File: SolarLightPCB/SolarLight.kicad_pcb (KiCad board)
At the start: 2 copper layers, 100 x 45 mm, 17 parts, among them J1 I2C, J2 SPI, U1 TP4056, U2 WeMos_D1_mini, U3 MCP1700-3302E

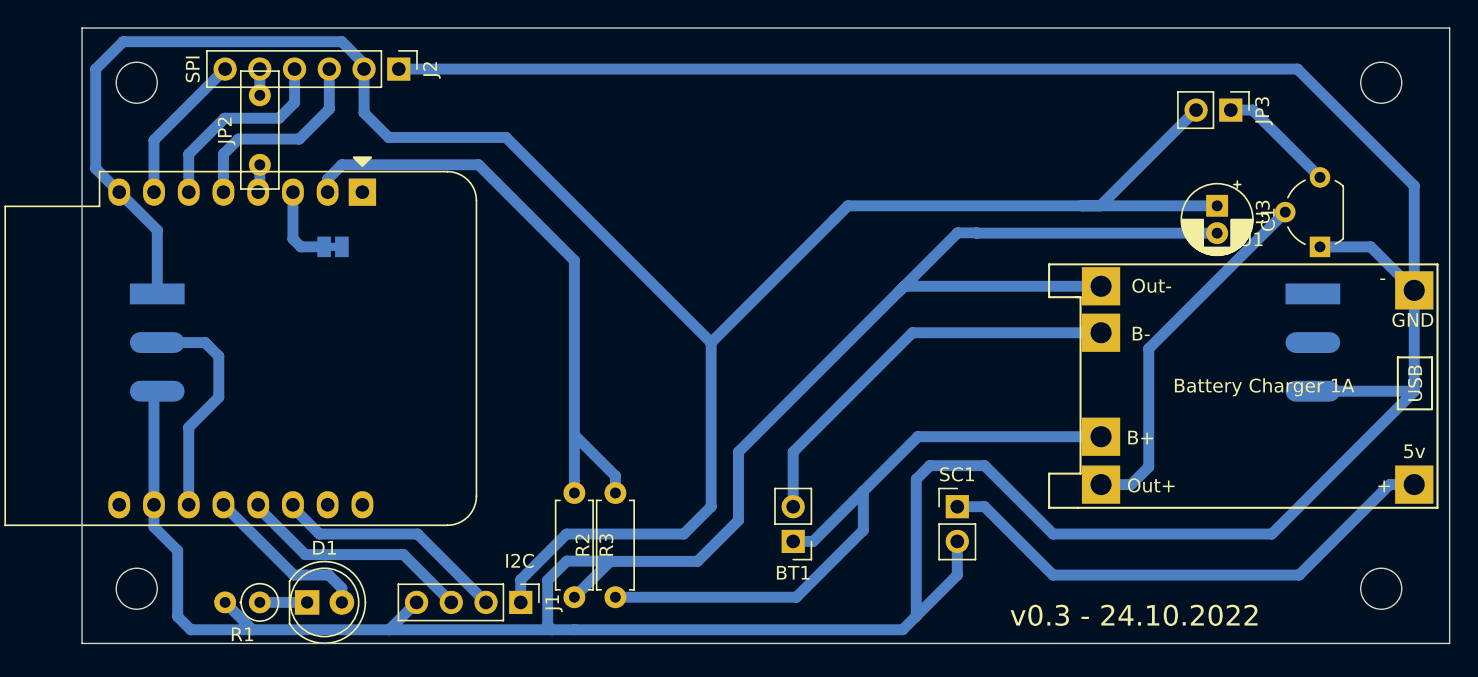
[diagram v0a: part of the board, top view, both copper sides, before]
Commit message: PCB Improvements
- Remove the LED
- Make the pads biggger
- Add a GND Plane
- Add a logo
- Connect both GND and VCC pads of the mechanical neopixel pin
- Align positive / negative pins of Battery and solar panel
- Make GND Pads rectangular
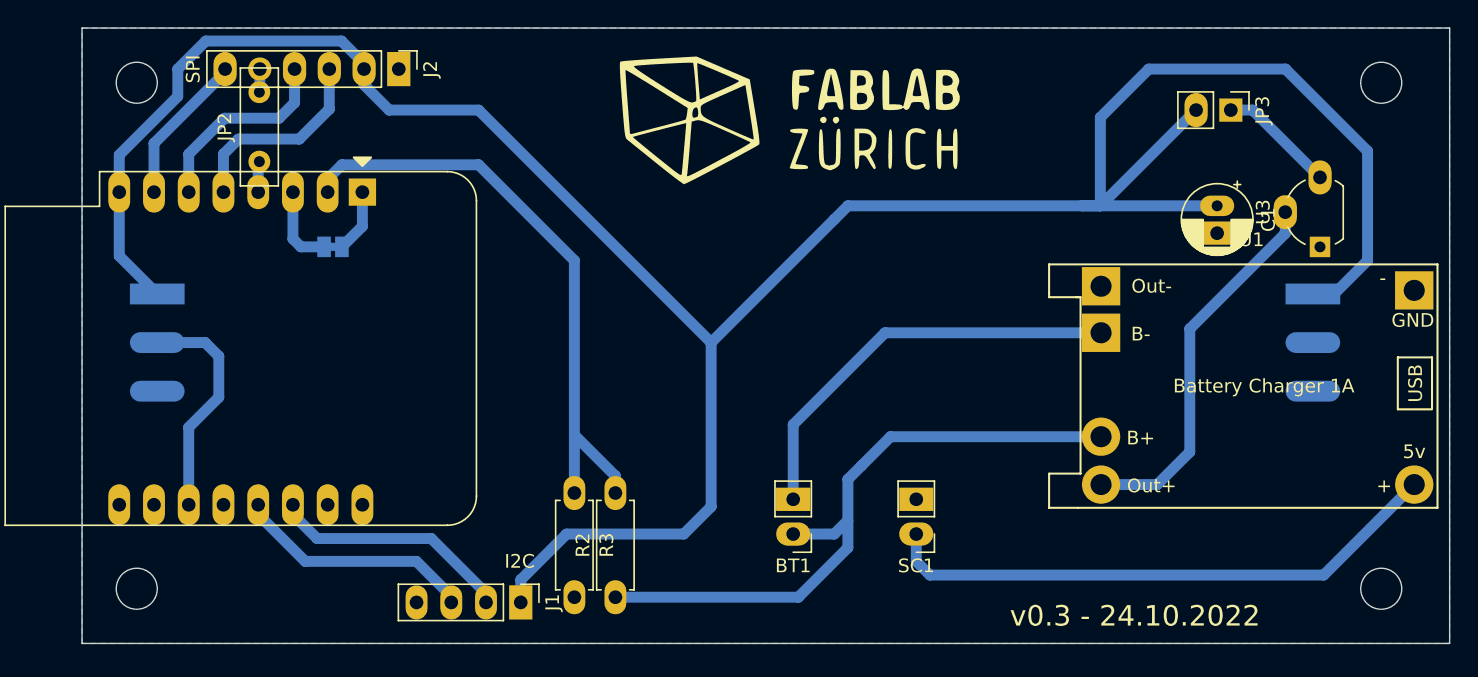
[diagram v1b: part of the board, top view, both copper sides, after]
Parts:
- removed D1: LED, LED_THT:LED_D5.0mm
- removed R1: R, Resistor_THT:R_Axial_DIN0207_L6.3mm_D2.5mm_P2.54mm_Vertical
- added G***: LOGO, LOGO, F.Cu at (132.0, 61.0)
- moved SC1 3.61 mm to (141.0, 92.0), turned to 180 degrees
- moved BT1 0.54 mm to (132.0, 92.0)
- moved JP2 0.23 mm to (93.0, 64.8)
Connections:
- LIN1 pad 1: unconnected-(LIN1-Pad1) -> +3V3
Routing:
- net GND: track 332.2 -> 0.00 mm
- net +3V3: track 157.9 -> 194.4 mm
- net LED: track 12.2 -> 0.00 mm
- net RST: track 0.71 -> 4.62 mm
- net Net-(D1-Pad1): track 3.46 -> 0.00 mm
- net Net-(SC1-Pad1): track 38.2 -> 41.6 mm
- net Net-(U1-Pad3): track 26.8 -> 27.9 mm
- net BATTERY: track 48.7 -> 47.7 mm
- net SCL: track 17.2 -> 17.9 mm
- net Net-(BT1-Pad2): track 30.1 -> 30.8 mm
- net SDA: track 17.2 -> 17.8 mm
- added copper zone on B.Cu, net GND

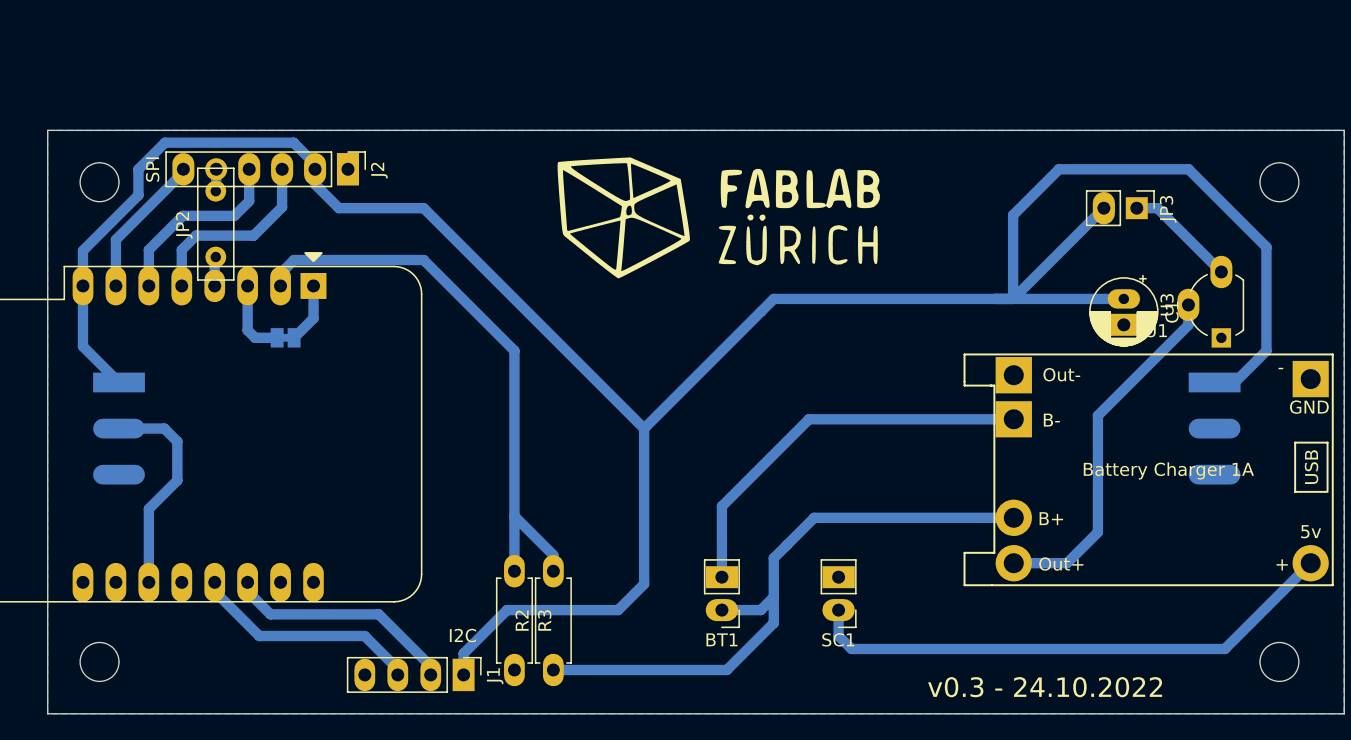
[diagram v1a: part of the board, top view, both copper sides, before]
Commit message: Move the SPI header
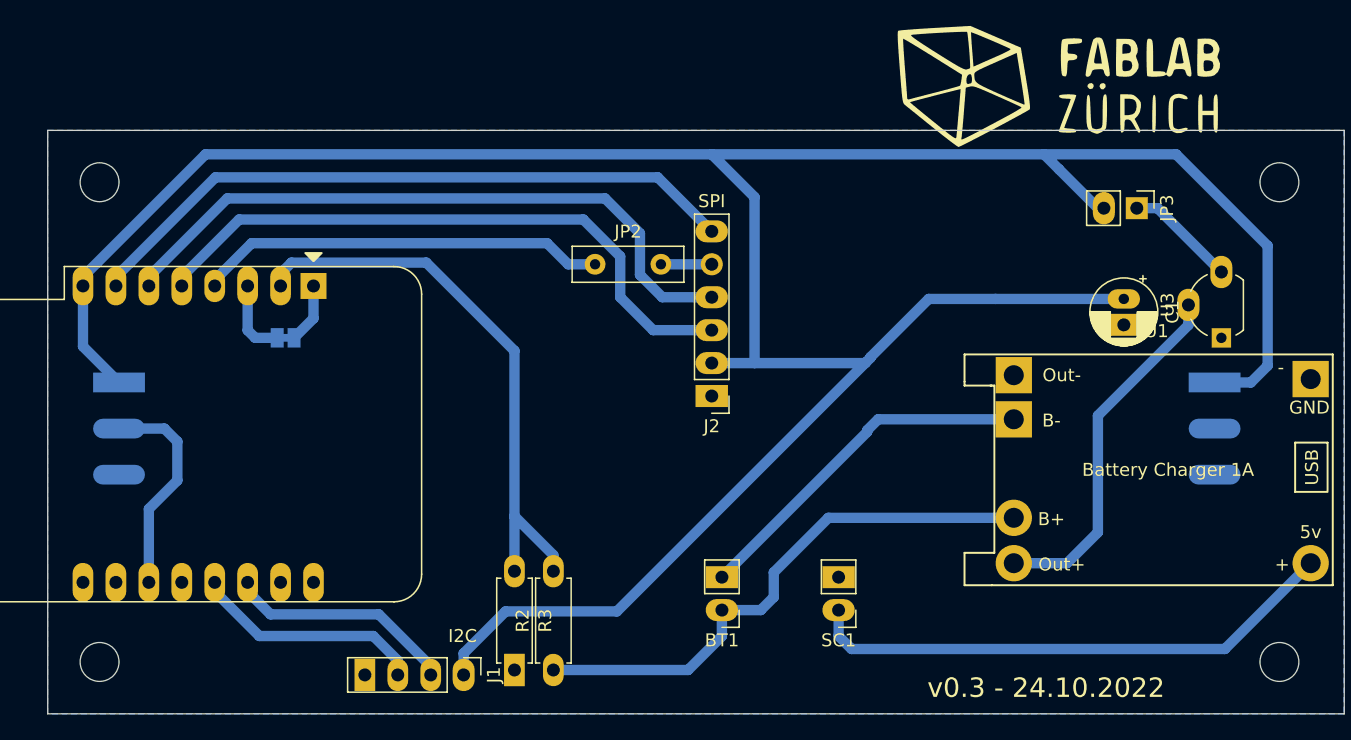
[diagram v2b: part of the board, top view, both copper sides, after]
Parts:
- moved J2 33.1 mm to (131.2, 75.5), turned to 180 degrees
- moved JP2 29.3 mm to (122.2, 65.3), turned to 0 degrees
- moved G*** 28.1 mm to (158.2, 50.9)
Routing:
- net CS: track 11.2 -> 51.6 mm
- net MOSI: track 14.5 -> 51.7 mm
- net MISO: track 14.8 -> 48.8 mm
- net SCK: track 2.26 -> 31.6 mm
- net +3V3: track 194.4 -> 221.0 mm
- net BATTERY: track 47.7 -> 42.7 mm
- net Net-(BT1-Pad2): track 30.8 -> 27.6 mm
- net Net-(J2-Pad5): track 1.92 -> 3.92 mm

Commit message: Cleanup some traces
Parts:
- moved G*** 17.2 mm to (146.2, 63.0)
- moved U2 5.65 mm to (106.1, 66.1)
- moved JP1 5.45 mm to (103.8, 70.6)
- moved R2 3.57 mm to (122.5, 97.0)
- moved R3 3.57 mm to (119.5, 89.4)
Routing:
- net SDA: track 18.1 -> 13.5 mm
- net MOSI: track 51.7 -> 47.2 mm
- net MISO: track 48.8 -> 44.4 mm
- net SCL: track 17.9 -> 13.6 mm
- net SCK: track 31.6 -> 27.5 mm
- net CS: track 51.6 -> 47.6 mm
- net A0: track 44.6 -> 47.9 mm
- net BATTERY: track 42.7 -> 43.8 mm
- net RST: track 4.62 -> 5.22 mm
- net Net-(JP1-Pad1): track 5.94 -> 5.43 mm

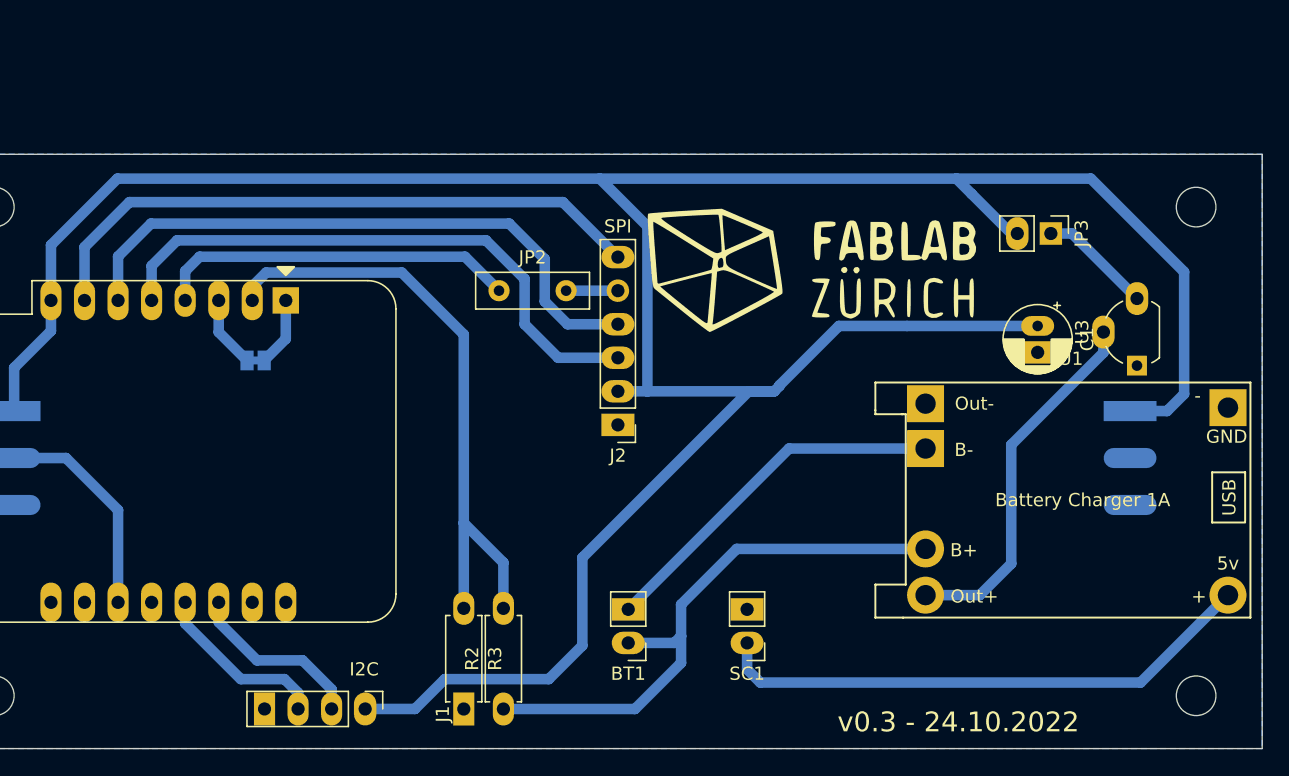
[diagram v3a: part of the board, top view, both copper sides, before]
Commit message: Add rotary encoder
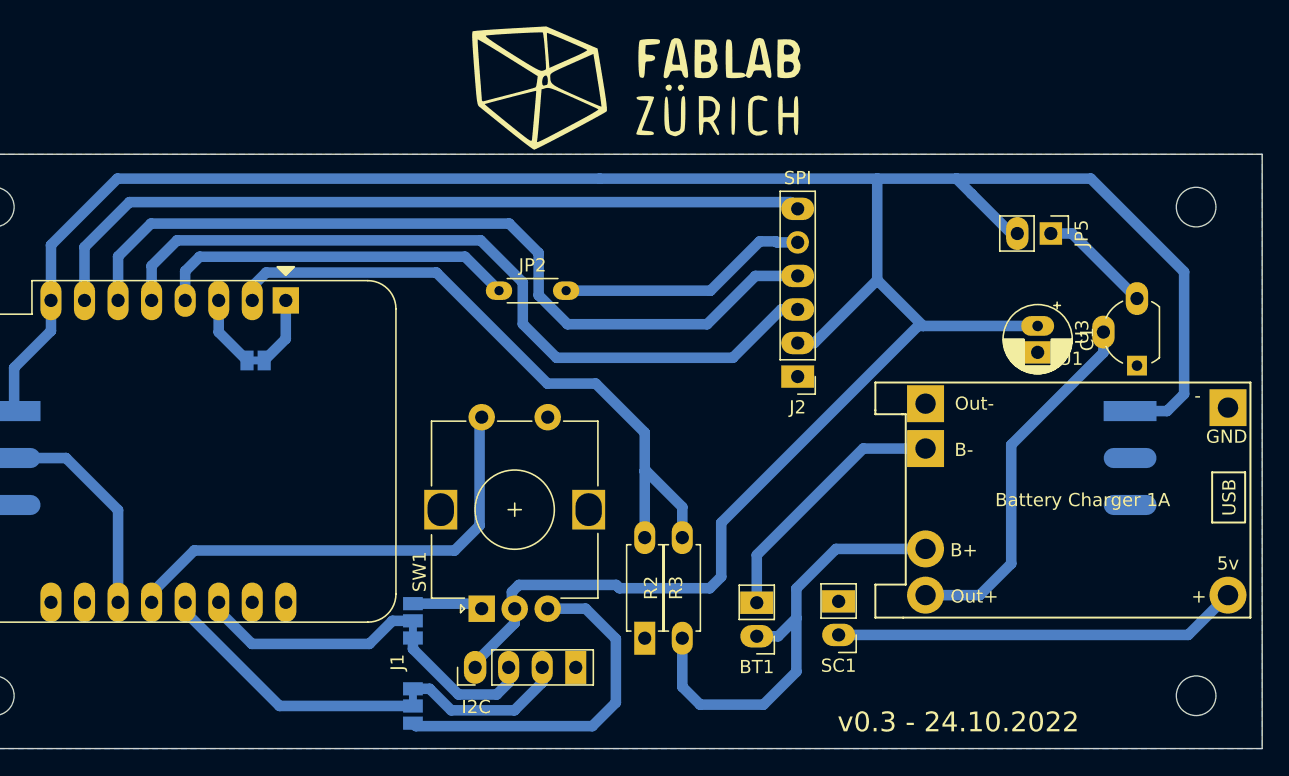
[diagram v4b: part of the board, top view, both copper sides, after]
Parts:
- added JP3: SolderJumper_3_Bridged12, Jumper:SolderJumper-3_P1.3mm_Bridged12_Pad1.0x1.5mm, B.Cu at (115.7, 96.8)
- added JP4: SolderJumper_3_Bridged12, Jumper:SolderJumper-3_P1.3mm_Bridged12_Pad1.0x1.5mm, B.Cu at (115.7, 90.3)
- added SW1: RotaryEncoder_Switch, Rotary_Encoder:RotaryEncoder_Alps_EC12E-Switch_Vertical_H20mm, F.Cu at (120.9, 89.4)
- JP2: value Bridge -> Jumper_2_Bridged; footprint Resistor_THT:R_Box_L8.4mm_W2.5mm_P5.08mm -> Resistor_THT:R_Axial_DIN0204_L3.6mm_D1.6mm_P5.08mm_Horizontal
- moved G*** 19.2 mm to (132.9, 49.2)
- moved R3 14.7 mm to (133.2, 84.0)
- moved R2 14.6 mm to (136.1, 91.6)
- moved J2 14.1 mm to (144.8, 71.8)
- moved BT1 9.75 mm to (141.7, 91.5)
- moved J1 8.90 mm to (120.4, 93.9), turned to 90 degrees
- moved SC1 6.96 mm to (147.9, 91.4)
- renumbered JP3 to JP5
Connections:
- U2 pad 12: LED -> ROTARY_SWITCH
- U2 pad 13: SDA -> Net-(U2-Pad13)
- U2 pad 14: SCL -> Net-(U2-Pad14)
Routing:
- net ROTARY_SWITCH: track 0.00 -> 35.9 mm
- net ROTARY_B: track 0.00 -> 27.1 mm
- net Net-(U2-Pad13): track 0.00 -> 20.9 mm
- net +3V3: track 221.0 -> 203.1 mm
- net Net-(U2-Pad14): track 0.00 -> 17.1 mm
- net Net-(J2-Pad5): track 3.92 -> 19.1 mm
- net MOSI: track 47.2 -> 62.4 mm
- net MISO: track 44.4 -> 59.4 mm
- net CS: track 47.6 -> 59.7 mm
- net Net-(SC1-Pad1): track 41.6 -> 30.7 mm
- net BATTERY: track 43.8 -> 34.8 mm
- net Net-(BT1-Pad2): track 27.6 -> 19.7 mm
- net ROTARY_A: track 0.00 -> 5.36 mm
- net SCL: track 13.6 -> 11.0 mm
- net A0: track 47.9 -> 50.5 mm
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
